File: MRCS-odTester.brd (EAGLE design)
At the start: 50 x 50 mm, 14 parts

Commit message: 1.1
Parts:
- added DCC, TRACK: (no value), SPCoast:MSTB2
- R1: value 15k -> 100k
- moved R1 12.7 mm to (28.6, 19.1)
- moved LED1 11.9 mm to (40.0, 40.0), turned to 90 degrees
- moved R4 11.8 mm to (33.0, 41.3), turned to 270 degrees
- moved SW1 11.4 mm to (28.6, 12.7)
- moved R2 7.62 mm to (17.1, 19.1)
- moved SW2 7.62 mm to (17.1, 12.7)
- moved C1 5.24 mm to (27.9, 27.9), turned to 270 degrees
- moved DCCOD 5.08 mm to (19.7, 41.3)
- moved R3 5.08 mm to (5.71, 19.1)
- moved SW3 5.08 mm to (4.45, 12.7)
- moved C2 4.02 mm to (19.7, 27.9), turned to 270 degrees
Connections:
- removed net TRACK+: DCCOD.2, SW1.1, SW1.2, SW2.1, SW2.2, SW3.1, SW3.2
- removed net TRACK-: DCCOD.4, R1.P$1, R2.P$1, R3.P$1
- new net DCC-COMMON: DCC.2, DCCOD.4
- new net DCC-FROMTRACK: DCCOD.2, SW1.1, SW1.2, SW2.1, SW2.2, SW3.1, SW3.2, TRACK.1
- new net DCC-TOTRACK: DCC.1, R1.P$1, R2.P$1, R3.P$1, TRACK.2
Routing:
- net DCC-FROMTRACK: track 0.00 -> 104.2 mm
- net TRACK+: track 82.3 -> 0.00 mm
- net DCC-TOTRACK: track 0.00 -> 63.2 mm
- net TRACK-: track 55.5 -> 0.00 mm
- net DCC-COMMON: track 0.00 -> 24.2 mm
- net +12V: track 45.7 -> 36.1 mm
- net N$5: track 5.08 -> 12.2 mm
- net VOUT: track 48.6 -> 41.6 mm
- net GND: track 43.8 -> 40.0 mm
- net N$1: track 9.72 -> 10.2 mm
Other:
- board text added: ""Too Low" and "Normal" lights mean Normal"
- board text added: "Adjust for Normal Detection and not "Too High""
- board text added: "DCCOD"
- board text added: "DCCOD Tester"
- board text added: "Go Bears!"
- board text added: "If all three light, the detector is too sensitive"
- board text added: "If only "too low" lights, the detector is not sensitive enough"
- board text added: "Made in the PCR, Coast Div, NMRA"
- board text added: "Model Railroading is Fun!"
- board text added: "Test"
- board text added: "Too HIGH"
- board text added: "Too LOW"
- board text added: "www.SPCoast.com"
- board text removed: "HIGH"
- board text removed: "LOW"
- board text removed: "Sensitivity"

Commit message: 2.0
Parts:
- BOARD1: value BOARD50X50 -> (none)
- C1: device SPCoast:E5-10.5 -> SPCoast:E3.5-10
- R1, R2, R3, R4: device SPCoast:AXIAL-0.3-RES -> SPCoast:AXIAL-0.4-RES
- moved R1 6.02 mm to (34.3, 21.0)
- moved R2 3.70 mm to (20.3, 21.0)
- moved R3 2.29 mm to (6.99, 21.0)
- moved R4 1.90 mm to (34.9, 41.3)
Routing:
- net DCC-TOTRACK: track 63.2 -> 58.6 mm
- net N$1: track 10.2 -> 12.7 mm
- net N$3: track 9.72 -> 11.5 mm
- net N$2: track 10.2 -> 11.7 mm
- net +12V: track 36.1 -> 37.3 mm
- net N$5: track 12.2 -> 11.6 mm
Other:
- board text added: ""Low" and "Normal" lights is a PASS"
- board text added: "2017-03"
- board text added: "Adjust for Normal Detection and not too High"
- board text added: "HIGH"
- board text added: "If only "low" lights, the detector is not sensitive enough"
- board text added: "LOW"
- board text added: "v2.0b"
- board text removed: ""Too Low" and "Normal" lights mean Normal"
- board text removed: "Adjust for Normal Detection and not "Too High""
- board text removed: "If only "too low" lights, the detector is not sensitive enough"
- board text removed: "Too HIGH"
- board text removed: "Too LOW"

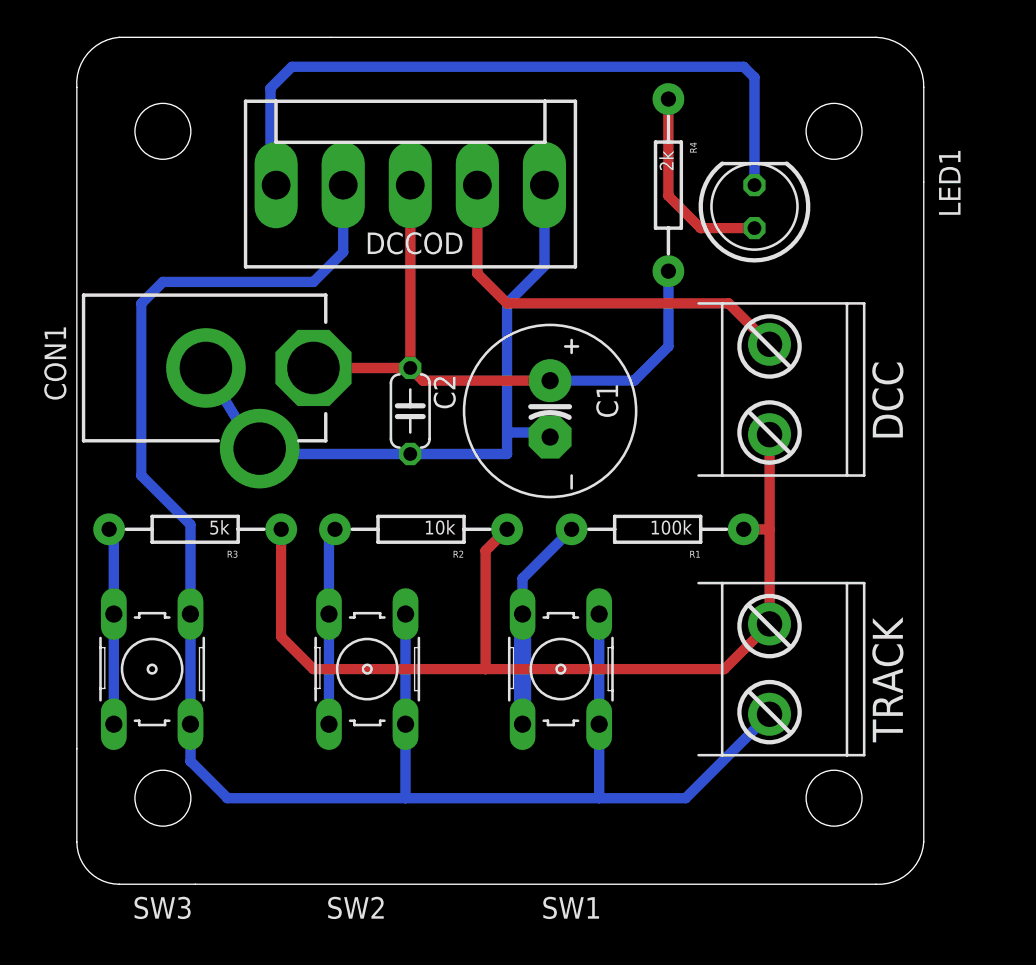
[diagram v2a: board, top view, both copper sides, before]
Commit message: silkscreen cleanup
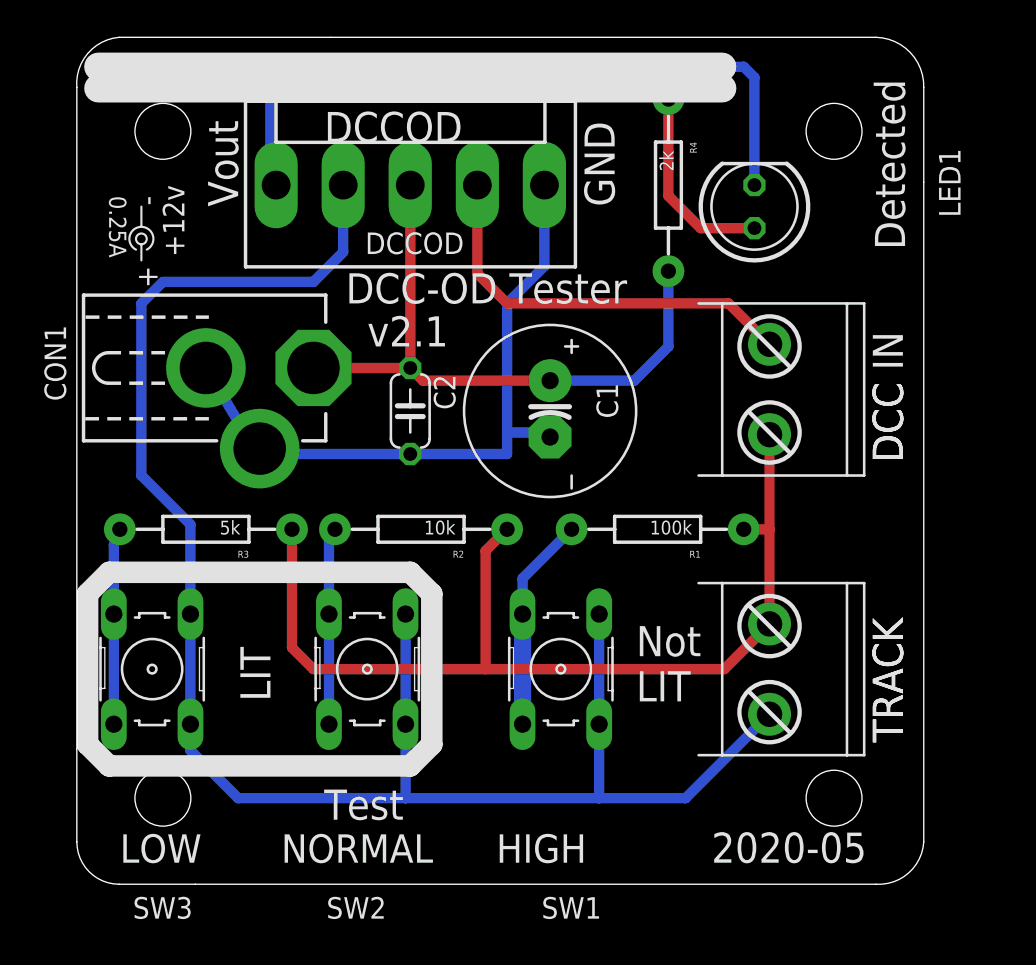
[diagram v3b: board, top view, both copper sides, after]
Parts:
- BOARD1: value (none) -> BOARD50X50
- U$1: device SPCoast:POWER_USAGE -> SPCoast:PWR_LABEL
- moved R3 0.63 mm to (7.62, 21.0)
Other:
- board text added: "2020-05"
- board text added: "DCC IN"
- board text added: "LIT"
- board text added: "Not LIT"
- board text added: "TRACK"
- board text added: "v2.1"
- board text removed: "2017-03"
- board text removed: "v2.0b"

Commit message: created 2x2 panel
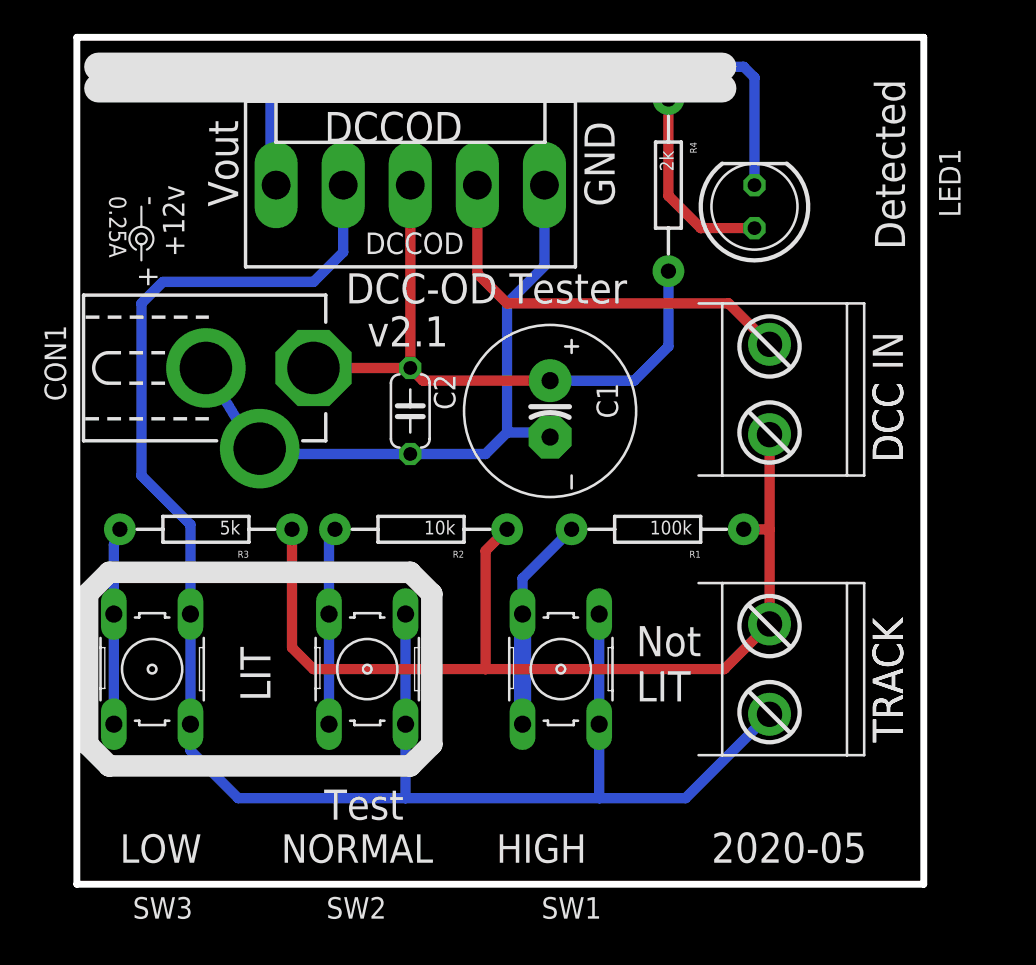
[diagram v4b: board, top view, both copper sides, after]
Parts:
- removed BOARD1: BOARD50X50, SPCoast:BOARD-SEEED5X5
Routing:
- net GND: track 40.1 -> 39.4 mm
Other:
- outline, holes or cut-outs redrawn
- board text added: "C1"
- board text added: "C2"
- board text added: "CON1"
- board text added: "DCC"
- board text added: "LED1"
- board text added: "R1"
- board text added: "R2"
- board text added: "R3"
- board text added: "R4"
- board text added: "SW1"
- board text added: "SW2"
- board text added: "SW3"
